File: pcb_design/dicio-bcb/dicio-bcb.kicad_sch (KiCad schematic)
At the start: 6 parts, among them J1 USB_C_Receptacle, J2 Conn_02x10_Odd_Even, J3 USB_C_Receptacle, J4 USB_C_Receptacle, J5 Conn_01x07

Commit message: Gerber exports
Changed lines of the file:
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@@
+    (stroke (width 0) (type default) (color 0 0 0 0))
+  )
+  (wire (pts (xy 226.06 38.1) (xy 234.95 38.1))
     (stroke (width 0) (type default) (color 0 0 0 0))
   )
@@
     (stroke (width 0) (type default) (color 0 0 0 0))
   )
+  (wire (pts (xy 226.06 29.21) (xy 234.95 29.21))
+    (stroke (width 0) (type default) (color 0 0 0 0))
+  )
   (wire (pts (xy 55.88 100.33) (xy 67.31 100.33))
     (stroke (width 0) (type default) (color 0 0 0 0))
@@
   (label "D+" (at 67.31 100.33 180)
     (effects (font (size 1.27 1.27)) (justify right bottom))
+  )
+  (symbol (lib_id "power:PWR_FLAG") (at 234.95 46.99 0) (unit 1)
+    (in_bom yes) (on_board yes) (fields_autoplaced)
+    (property "Reference" "#FLG01" (id 0) (at 234.95 45.085 0)
+      (effects (font (size 1.27 1.27)) hide)
+    )
+    (property "Value" "PWR_FLAG" (id 1) (at 234.95 41.91 0))
+    (property "Footprint" "" (id 2) (at 234.95 46.99 0)
+      (effects (font (size 1.27 1.27)) hide)
+    )
+    (property "Datasheet" "~" (id 3) (at 234.95 46.99 0)
+      (effects (font (size 1.27 1.27)) hide)
+    )
+    (pin "1")
+  )
+  (symbol (lib_id "power:VBUS") (at 226.06 29.21 0) (unit 1)
+    (in_bom yes) (on_board yes) (fields_autoplaced)
+    (property "Reference" "#PWR0103" (id 0) (at 226.06 33.02 0)
+      (effects (font (size 1.27 1.27)) hide)
+    )
+    (property "Value" "VBUS" (id 1) (at 226.06 24.13 0))
+    (property "Footprint" "" (id 2) (at 226.06 29.21 0)
+      (effects (font (size 1.27 1.27)) hide)
+    )
+    (property "Datasheet" "" (id 3) (at 226.06 29.21 0)
+      (effects (font (size 1.27 1.27)) hide)
+    )
+    (pin "1")
   )
   (symbol (lib_id "power:GND") (at 113.03 146.05 0) (unit 1)
@@
     (pin "1")
   )
+  (symbol (lib_id "power:GND") (at 234.95 46.99 0) (unit 1)
+    (in_bom yes) (on_board yes) (fields_autoplaced)
+    (property "Reference" "#PWR09" (id 0) (at 234.95 53.34 0)
+      (effects (font (size 1.27 1.27)) hide)
+    )
+    (property "Value" "GND" (id 1) (at 234.95 52.07 0))
+    (property "Footprint" "" (id 2) (at 234.95 46.99 0)
+      (effects (font (size 1.27 1.27)) hide)
+    )
+    (property "Datasheet" "" (id 3) (at 234.95 46.99 0)
+      (effects (font (size 1.27 1.27)) hide)
+    )
+    (pin "1")
+  )
+  (symbol (lib_id "power:PWR_FLAG") (at 234.95 38.1 0) (unit 1)
+    (in_bom yes) (on_board yes) (fields_autoplaced)
+    (property "Reference" "#FLG0102" (id 0) (at 234.95 36.195 0)
+      (effects (font (size 1.27 1.27)) hide)
+    )
+    (property "Value" "PWR_FLAG" (id 1) (at 234.95 33.02 0))
+    (property "Footprint" "" (id 2) (at 234.95 38.1 0)
+      (effects (font (size 1.27 1.27)) hide)
+    )
+    (property "Datasheet" "~" (id 3) (at 234.95 38.1 0)
+      (effects (font (size 1.27 1.27)) hide)
+    )
+    (pin "1")
+  )
+  (symbol (lib_id "power:PWR_FLAG") (at 234.95 29.21 0) (unit 1)
+    (in_bom yes) (on_board yes) (fields_autoplaced)
+    (property "Reference" "#FLG0101" (id 0) (at 234.95 27.305 0)
+      (effects (font (size 1.27 1.27)) hide)
+    )
+    (property "Value" "PWR_FLAG" (id 1) (at 234.95 24.13 0))
+    (property "Footprint" "" (id 2) (at 234.95 29.21 0)
+      (effects (font (size 1.27 1.27)) hide)
+    )
+    (property "Datasheet" "~" (id 3) (at 234.95 29.21 0)
+      (effects (font (size 1.27 1.27)) hide)
+    )
+    (pin "1")
+  )
   (symbol (lib_id "power:VBUS") (at 66.04 57.15 180) (unit 1)
     (in_bom yes) (on_board yes) (fields_autoplaced)
@@
     (pin "S1")
   )
+  (symbol (lib_id "power:+3.3V") (at 226.06 38.1 0) (unit 1)
+    (in_bom yes) (on_board yes) (fields_autoplaced)
+    (property "Reference" "#PWR0104" (id 0) (at 226.06 41.91 0)
+      (effects (font (size 1.27 1.27)) hide)
+    )
+    (property "Value" "+3.3V" (id 1) (at 226.06 33.02 0))
+    (property "Footprint" "" (id 2) (at 226.06 38.1 0)
+      (effects (font (size 1.27 1.27)) hide)
+    )
+    (property "Datasheet" "" (id 3) (at 226.06 38.1 0)
+      (effects (font (size 1.27 1.27)) hide)
+    )
+    (pin "1")
+  )
   (sheet_instances
     (path "/" (page "1"))
   )
   (symbol_instances
+    (path "/0115f7b3-04e5-4b85-879c-091a2fd79678"
+      (reference "#FLG01") (unit 1) (value "PWR_FLAG") (footprint "")
+    )
+    (path "/a161eb58-7b15-4d30-9098-d3cba48604cc"
+      (reference "#FLG0101") (unit 1) (value "PWR_FLAG") (footprint "")
+    )
+    (path "/9961cfb4-404c-4d56-a29d-4dec9b94f865"
+      (reference "#FLG0102") (unit 1) (value "PWR_FLAG") (footprint "")
+    )
     (path "/a4b29170-da92-4266-8b02-0a492c4d934f"
       (reference "#PWR01") (unit 1) (value "VBUS") (footprint "")
@@
       (reference "#PWR08") (unit 1) (value "VBUS") (footprint "")
     )
+    (path "/8e13717c-c97c-4270-b904-c8ce337e310e"
+      (reference "#PWR09") (unit 1) (value "GND") (footprint "")
+    )
     (path "/d7111bcb-8726-4c91-bf1c-f10489b7a090"
       (reference "#PWR0101") (unit 1) (value "+3.3V") (footprint "")
@@
       (reference "#PWR0102") (unit 1) (value "GND") (footprint "")
     )
+    (path "/13e52b84-f473-4cdb-90bc-9dff9d8b2b6e"
+      (reference "#PWR0103") (unit 1) (value "VBUS") (footprint "")
+    )
+    (path "/f10104c6-642a-48a3-b14f-fc37a67fef61"
+      (reference "#PWR0104") (unit 1) (value "+3.3V") (footprint "")
+    )
     (path "/e2da200a-c1d6-4a7f-80b7-f5e023051d77"

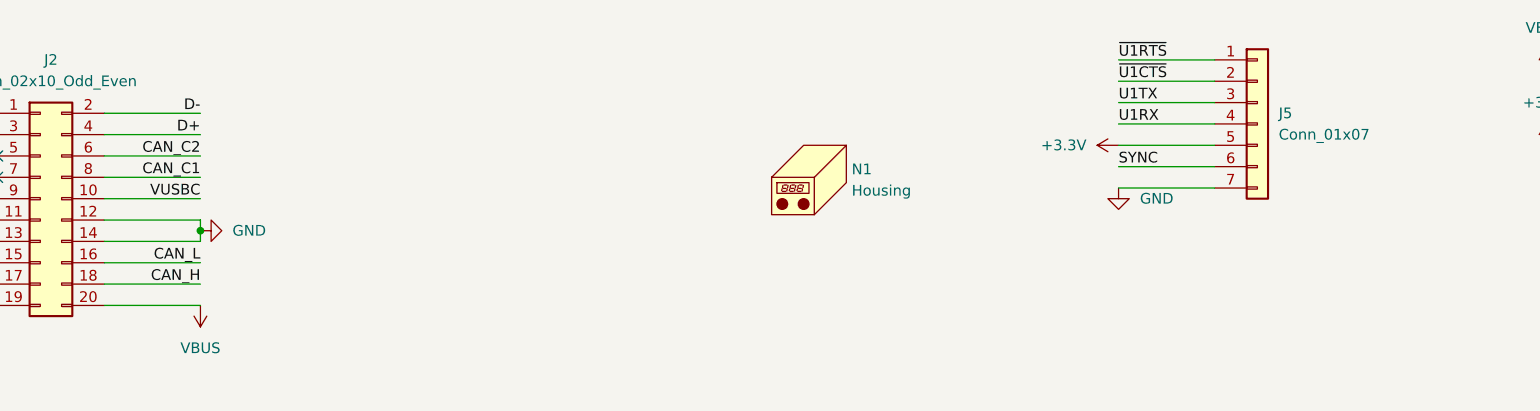
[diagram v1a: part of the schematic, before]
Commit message: Expose RTCC pin for synchronisation
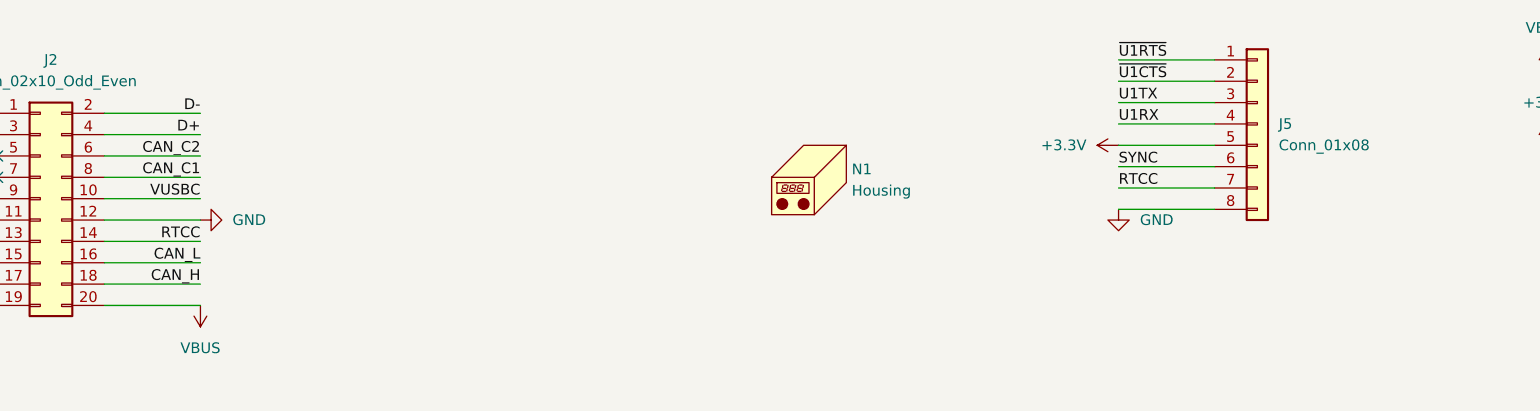
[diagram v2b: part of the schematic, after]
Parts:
- removed J5: Conn_01x07, Connector_PinHeader_2.54mm:PinHeader_1x07_P2.54mm_Vertical, symbol Connector_Generic:Conn_01x07
- added J5: Conn_01x08, Connector_PinHeader_2.54mm:PinHeader_1x08_P2.54mm_Vertical, symbol Connector_Generic:Conn_01x08
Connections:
- net +3.3V: now also J5.5 (Pin_5)
- net GND: now also J5.8 (Pin_8); no longer J2.14 (Pin_14)
- net SYNC: now also J5.6 (Pin_6)
- net U1RX: now also J5.4 (Pin_4)
- net U1TX: now also J5.3 (Pin_3)
- net ~{U1CTS}: now also J5.2 (Pin_2)
- net ~{U1RTS}: now also J5.1 (Pin_1)
- new net RTCC: J2.14 (Pin_14), J5.7 (Pin_7)
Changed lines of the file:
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@@
   (junction (at 167.64 146.05) (diameter 0) (color 0 0 0 0)
-  )
-  (junction (at 66.04 48.26) (diameter 0) (color 0 0 0 0)
   )
   (no_connect (at 55.88 138.43))
@@
     (stroke (width 0) (type default) (color 0 0 0 0))
   )
+  (wire (pts (xy 175.26 45.72) (xy 186.69 45.72))
+    (stroke (width 0) (type default) (color 0 0 0 0))
+  )
   (wire (pts (xy 66.04 52.07) (xy 54.61 52.07))
     (stroke (width 0) (type default) (color 0 0 0 0))
@@
     (stroke (width 0) (type default) (color 0 0 0 0))
   )
-  (wire (pts (xy 66.04 48.26) (xy 66.04 46.99))
-    (stroke (width 0) (type default) (color 0 0 0 0))
-  )
   (wire (pts (xy 186.69 80.01) (xy 198.12 80.01))
     (stroke (width 0) (type default) (color 0 0 0 0))
@@
     (stroke (width 0) (type default) (color 0 0 0 0))
   )
-  (wire (pts (xy 66.04 49.53) (xy 66.04 48.26))
-    (stroke (width 0) (type default) (color 0 0 0 0))
-  )
   (wire (pts (xy 167.64 146.05) (xy 171.45 146.05))
     (stroke (width 0) (type default) (color 0 0 0 0))
@@
     (effects (font (size 1.27 1.27)) (justify right bottom))
   )
+  (label "RTCC" (at 175.26 43.18 0)
+    (effects (font (size 1.27 1.27)) (justify left bottom))
+  )
   (label "CAN_L" (at 198.12 95.25 180)
     (effects (font (size 1.27 1.27)) (justify right bottom))
@@
   (label "~{U1CTS}" (at 175.26 30.48 0)
     (effects (font (size 1.27 1.27)) (justify left bottom))
+  )
+  (label "RTCC" (at 66.04 49.53 180)
+    (effects (font (size 1.27 1.27)) (justify right bottom))
   )
   (label "CAN_L" (at 143.51 95.25 180)
@@
     (pin "1")
   )
-  (symbol (lib_id "Connector_Generic:Conn_01x07") (at 191.77 35.56 0) (unit 1)
-    (in_bom yes) (on_board yes) (fields_autoplaced)
-    (property "Reference" "J5" (id 0) (at 194.31 34.2899 0)
-      (effects (font (size 1.27 1.27)) (justify left))
-    )
-    (property "Value" "Conn_01x07" (id 1) (at 194.31 36.8299 0)
-      (effects (font (size 1.27 1.27)) (justify left))
-    )
-    (property "Footprint" "Connector_PinHeader_2.54mm:PinHeader_1x07_P2.54mm_Vertical" (id 2) (at 191.77 35.56 0)
-      (effects (font (size 1.27 1.27)) hide)
-    )
-    (property "Datasheet" "~" (id 3) (at 191.77 35.56 0)
-      (effects (font (size 1.27 1.27)) hide)
-    )
-    (pin "1")
-    (pin "2")
-    (pin "3")
-    (pin "4")
-    (pin "5")
-    (pin "6")
-    (pin "7")
-  )
   (symbol (lib_id "power:+3.3V") (at 30.48 46.99 90) (unit 1)
     (in_bom yes) (on_board yes) (fields_autoplaced)
@@
     (pin "1")
   )
-  (symbol (lib_id "power:GND") (at 175.26 43.18 0) (unit 1)
-    (in_bom yes) (on_board yes) (fields_autoplaced)
-    (property "Reference" "#PWR0102" (id 0) (at 175.26 49.53 0)
-      (effects (font (size 1.27 1.27)) hide)
-    )
-    (property "Value" "GND" (id 1) (at 177.8 44.4499 0)
+  (symbol (lib_id "power:GND") (at 175.26 45.72 0) (unit 1)
+    (in_bom yes) (on_board yes) (fields_autoplaced)
+    (property "Reference" "#PWR0102" (id 0) (at 175.26 52.07 0)
+      (effects (font (size 1.27 1.27)) hide)
+    )
+    (property "Value" "GND" (id 1) (at 177.8 46.9899 0)
       (effects (font (size 1.27 1.27)) (justify left))
     )
-    (property "Footprint" "" (id 2) (at 175.26 43.18 0)
-      (effects (font (size 1.27 1.27)) hide)
-    )
-    (property "Datasheet" "" (id 3) (at 175.26 43.18 0)
+    (property "Footprint" "" (id 2) (at 175.26 45.72 0)
+      (effects (font (size 1.27 1.27)) hide)
+    )
+    (property "Datasheet" "" (id 3) (at 175.26 45.72 0)
       (effects (font (size 1.27 1.27)) hide)
     )
@@
     (pin "1")
   )
-  (symbol (lib_id "power:GND") (at 66.04 48.26 90) (unit 1)
-    (in_bom yes) (on_board yes) (fields_autoplaced)
-    (property "Reference" "#PWR02" (id 0) (at 72.39 48.26 0)
-      (effects (font (size 1.27 1.27)) hide)
-    )
-    (property "Value" "GND" (id 1) (at 69.85 48.2601 90)
+  (symbol (lib_id "power:GND") (at 66.04 46.99 90) (unit 1)
+    (in_bom yes) (on_board yes) (fields_autoplaced)
+    (property "Reference" "#PWR02" (id 0) (at 72.39 46.99 0)
+      (effects (font (size 1.27 1.27)) hide)
+    )
+    (property "Value" "GND" (id 1) (at 69.85 46.9901 90)
       (effects (font (size 1.27 1.27)) (justify right))
     )
-    (property "Footprint" "" (id 2) (at 66.04 48.26 0)
-      (effects (font (size 1.27 1.27)) hide)
-    )
-    (property "Datasheet" "" (id 3) (at 66.04 48.26 0)
+    (property "Footprint" "" (id 2) (at 66.04 46.99 0)
+      (effects (font (size 1.27 1.27)) hide)
+    )
+    (property "Datasheet" "" (id 3) (at 66.04 46.99 0)
       (effects (font (size 1.27 1.27)) hide)
     )
@@
     (pin "1")
   )
+  (symbol (lib_id "Connector_Generic:Conn_01x08") (at 191.77 35.56 0) (unit 1)
+    (in_bom yes) (on_board yes) (fields_autoplaced)
+    (property "Reference" "J5" (id 0) (at 194.31 35.5599 0)
+      (effects (font (size 1.27 1.27)) (justify left))
+    )
+    (property "Value" "Conn_01x08" (id 1) (at 194.31 38.0999 0)
+      (effects (font (size 1.27 1.27)) (justify left))
+    )
+    (property "Footprint" "Connector_PinHeader_2.54mm:PinHeader_1x08_P2.54mm_Vertical" (id 2) (at 191.77 35.56 0)
+      (effects (font (size 1.27 1.27)) hide)
+    )
+    (property "Datasheet" "~" (id 3) (at 191.77 35.56 0)
+      (effects (font (size 1.27 1.27)) hide)
+    )
+    (pin "1")
+    (pin "2")
+    (pin "3")
+    (pin "4")
+    (pin "5")
+    (pin "6")
+    (pin "7")
+    (pin "8")
+  )
   (sheet_instances
     (path "/" (page "1"))
@@
       (reference "J4") (unit 1) (value "USB_C_Receptacle") (footprint "custom_footprints:USB_C_Receptacle_Amphenol_12401861XX12A")
     )
-    (path "/4ce2321a-af08-4cf9-a194-8db0cea94a75"
-      (reference "J5") (unit 1) (value "Conn_01x07") (footprint "Connector_PinHeader_2.54mm:PinHeader_1x07_P2.54mm_Vertical")
+    (path "/f56c0987-cf3e-451c-a503-b1c75822f0d0"
+      (reference "J5") (unit 1) (value "Conn_01x08") (footprint "Connector_PinHeader_2.54mm:PinHeader_1x08_P2.54mm_Vertical")
     )
     (path "/2c376c53-db01-4dfc-9b20-4fa299a33bd0"

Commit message: Various updates for Aisler order.
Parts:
- J1, J3, J4: MPN (none) -> 124018612112A; Manufacturer (none) -> Amphenol
- J2: MPN (none) -> MMS-110-02-F-DV; Manufacturer (none) -> Samtec
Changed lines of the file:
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@@
+      (effects (font (size 1.27 1.27)) hide)
+    )
+    (property "MPN" "124018612112A" (id 4) (at 171.45 105.41 0)
+      (effects (font (size 1.27 1.27)) hide)
+    )
+    (property "Manufacturer" "Amphenol" (id 5) (at 171.45 105.41 0)
       (effects (font (size 1.27 1.27)) hide)
     )
@@
       (effects (font (size 1.27 1.27)) hide)
     )
+    (property "MPN" "124018612112A" (id 4) (at 116.84 105.41 0)
+      (effects (font (size 1.27 1.27)) hide)
+    )
+    (property "Manufacturer" "Amphenol" (id 5) (at 116.84 105.41 0)
+      (effects (font (size 1.27 1.27)) hide)
+    )
     (pin "A1")
     (pin "A10")
@@
       (effects (font (size 1.27 1.27)) hide)
     )
+    (property "MPN" "MMS-110-02-F-DV" (id 4) (at 46.99 44.45 0)
+      (effects (font (size 1.27 1.27)) hide)
+    )
+    (property "Manufacturer" "Samtec" (id 5) (at 46.99 44.45 0)
+      (effects (font (size 1.27 1.27)) hide)
+    )
     (pin "1")
     (pin "10")
@@
       (effects (font (size 1.27 1.27)) hide)
     )
+    (property "MPN" "124018612112A" (id 4) (at 40.64 105.41 0)
+      (effects (font (size 1.27 1.27)) hide)
+    )
+    (property "Manufacturer" "Amphenol" (id 5) (at 40.64 105.41 0)
+      (effects (font (size 1.27 1.27)) hide)
+    )
